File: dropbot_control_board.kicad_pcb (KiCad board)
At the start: 4 copper layers, 84 x 92 mm, 130 parts, among them IC1 MCP6024, J1 TFM-105-02-X-DH, P1 CONN_01X01, P2 CONN_01X01, P3 CONN_01X04, P4 CONN_01X04, P5 CONN_01X01, P7 CONN_01X04, P8 CONN_01X03, Q1 STP33N65M2, Q5 IRF740BPBF, Q6 IRF740BPBF, U1 Teensy_3.2, U10 W25Q64FV, U2 MAX1771, U3 CAT5171, U4 HV7802, U5 DPST (2 Form A), 350V, U6 NCP5304, U7 DPST (2 Form A), 350V, U8 DPST (2 Form A), 350V, U9 74AHC1G32

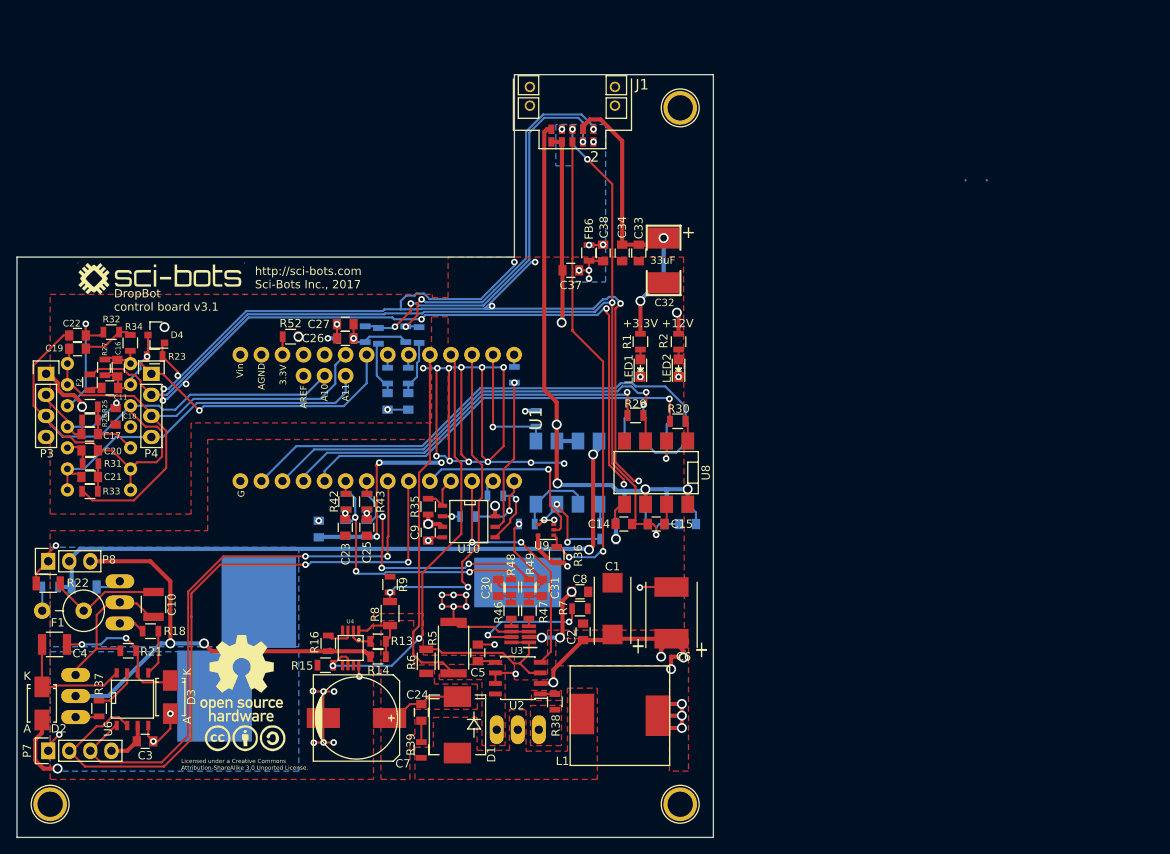
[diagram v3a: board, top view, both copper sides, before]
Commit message: Add usb passthrough, reset button, ...
* add usb passthrough
* add reset button
* fix bad trace on U5
* fix part number for C7 (3.3uF instead of 10uF)
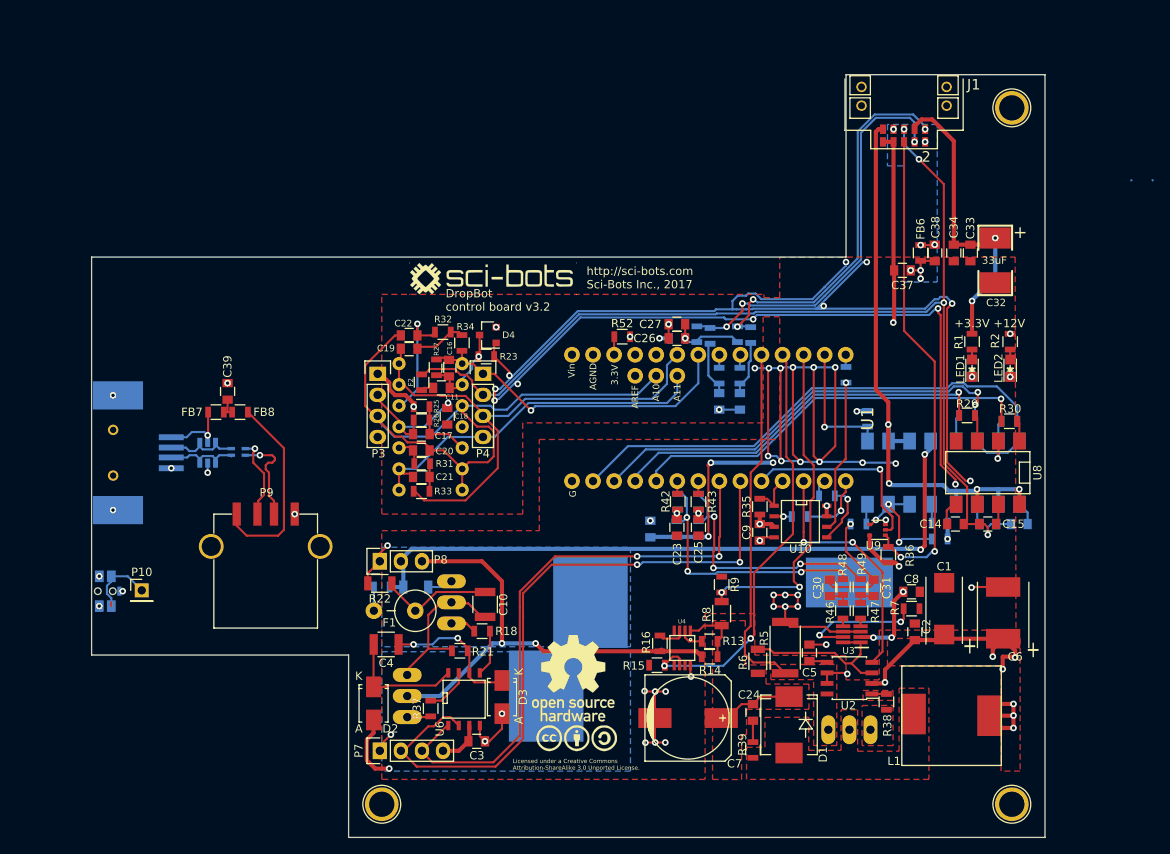
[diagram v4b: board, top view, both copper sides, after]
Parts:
- added C39: 0.1uF, Capacitors_SMD:C_0805, F.Cu at (49.4, 59.2)
- added D5: WE-TVS_824015, WheelerLab:wurth-WE-TVS_SOT23-6L, B.Cu at (47.0, 66.6)
- added FB7: 600 Ohm@100MHz, Resistors_SMD:R_0805, F.Cu at (48.0, 61.7)
- added FB8: 600 Ohm@100MHz, Resistors_SMD:R_0805, F.Cu at (50.9, 61.7)
- added L2: 90 Ohm@100MHz, WheelerLab:wurth-WE-CNSW_0805, B.Cu at (50.7, 66.5)
- added P10: CONN_01X01, Pin_Headers:Pin_Header_Straight_1x01_Pitch2.54mm, F.Cu at (39.0, 83.2)
- added P6: USB_B, WheelerLab:1734346-1, B.Cu at (35.6, 66.6)
- added P9: USB_A, WheelerLab:AU-Y1006, F.Cu at (54.0, 74.0)
- added SW1: PROG, WheelerLab:PTS840_GK_SMTR_LFS, B.Cu at (34.6, 83.3)
- C23, C25, C30, C31: value C_Small -> C
- R19, R20, R3, R4: value 4.75k -> 2k
- R40, R41, R42, R43, R44, R45, R46, R47, R48, R49, R50, R51: value R -> 0R
- moved C2 40.0 mm to (132.3, 88.2), turned to 270 degrees
- moved C37 40.0 mm to (130.8, 44.6)
- moved LED2 40.0 mm to (143.8, 56.4)
- moved R10 40.0 mm to (135.3, 77.0)
- moved R12 40.0 mm to (135.3, 75.1)
- moved R2 40.0 mm to (143.8, 53.2)
- moved C18 40.0 mm to (75.9, 62.2)
- moved C36 40.0 mm to (100.4, 75.8)
- moved G*** 40.0 mm to (81.4, 45.6)
- moved Q6 40.0 mm to (76.4, 84.6)
- moved R16 40.0 mm to (101.5, 89.6)
- moved R31 40.0 mm to (72.9, 67.9)
- moved R32 40.0 mm to (75.4, 52.0)
- moved R37 40.0 mm to (73.9, 97.5)
- moved U6 40.0 mm to (77.9, 96.3)
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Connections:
- C2 pad 1: +12V -> GND
- C2 pad 2: GND -> +12V
- U5 pad 2: Net-(R11-Pad2) -> Net-(R10-Pad2)
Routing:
- net Net-(FB8-Pad2): track 0.00 -> 23.9 mm
- net D+: track 0.00 -> 11.9 mm, vias 0 -> 1
- net Net-(D5-Pad4): track 0.00 -> 10.5 mm
- net CHASIS_GND: track 1.77 -> 12.1 mm, vias 2 -> 10
- net D-: track 0.00 -> 10.0 mm, vias 0 -> 1
- net Net-(D5-Pad1): track 0.00 -> 9.96 mm
- net Net-(D5-Pad5): track 0.00 -> 8.49 mm, vias 0 -> 1
- net Net-(P10-Pad1): track 0.00 -> 8.41 mm
- net Net-(R11-Pad2): track 9.47 -> 2.45 mm
- net +12V: track 82.3 -> 79.7 mm
- net Net-(R10-Pad2): track 12.9 -> 15.4 mm
- net Net-(C39-Pad2): track 0.00 -> 2.50 mm
- net GND: vias 47 -> 48
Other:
- board size 84 x 92 mm -> 115 x 92 mm
- net class PWR: via_dia 1.2 -> 0.8; via_drill 0.8 -> 0.4
- board text added: "DropBot control board v3.2"
- board text removed: "DropBot control board v3.1"

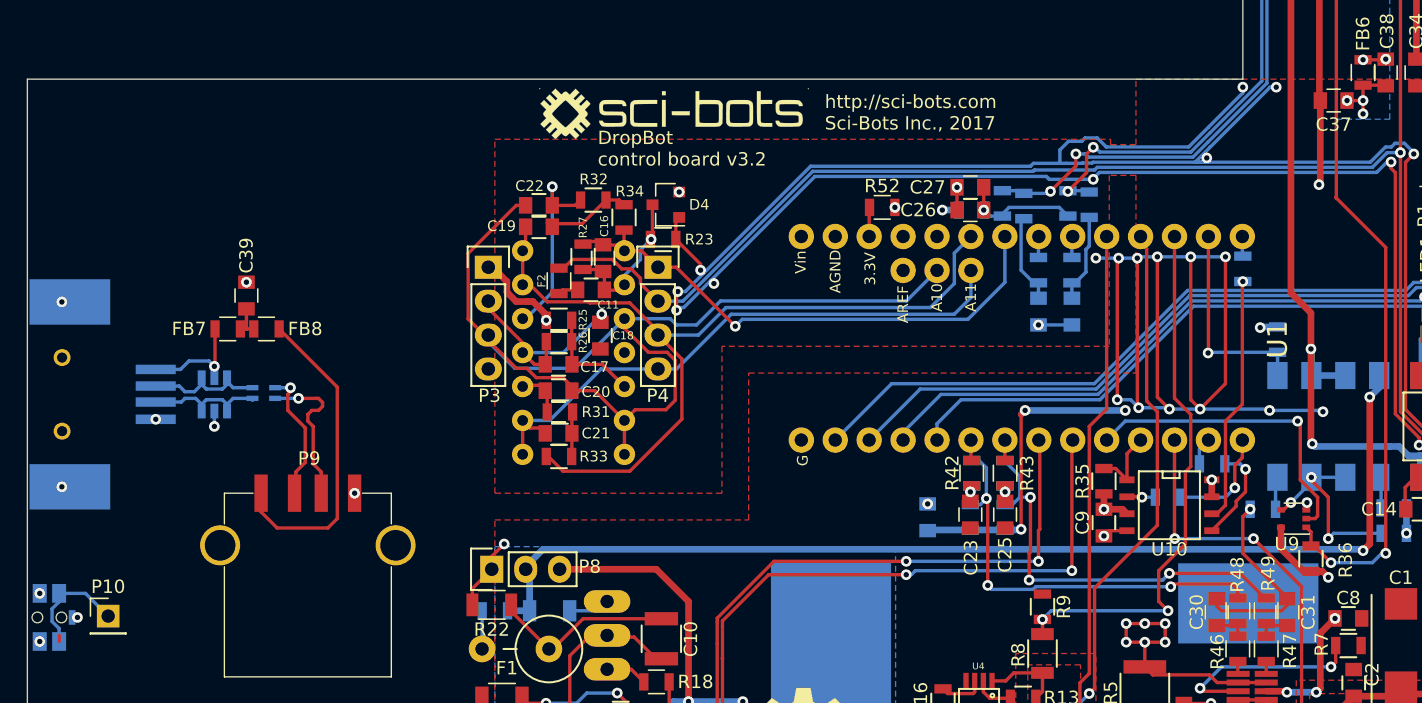
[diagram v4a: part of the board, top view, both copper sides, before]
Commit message: Swap F2 for higher voltage rating, monitor HV_OE
* swap F2 for 1210 footprint: B59807A90A62 (higher voltage rating)
* monitor HV_OE with A8
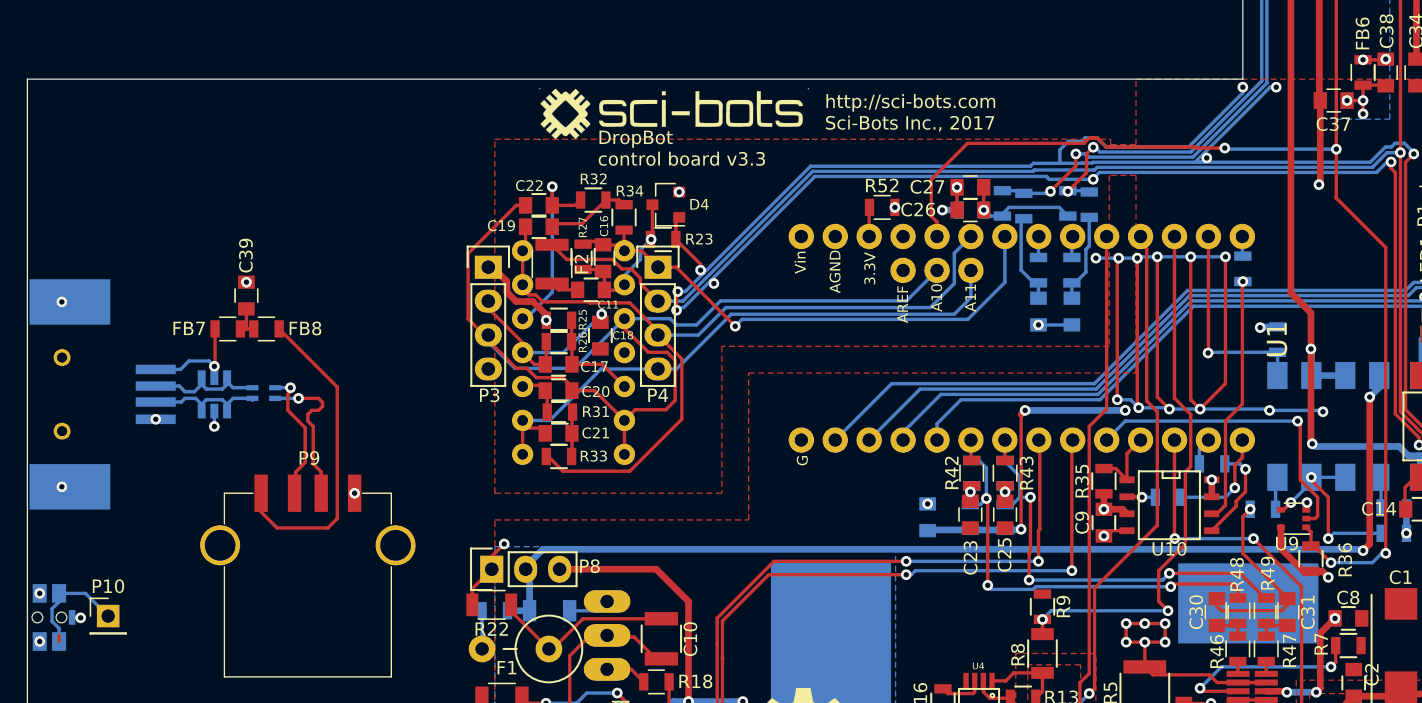
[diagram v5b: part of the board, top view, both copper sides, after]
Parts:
- F2: footprint Resistors_SMD:R_0805 -> Resistors_SMD:R_1210
- moved F2 1.35 mm to (72.3, 56.9)
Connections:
- U1 pad 22: Net-(U1-Pad22) -> HV_OE
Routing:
- net HV_OE: track 59.2 -> 95.6 mm, vias 2 -> 4
- net Net-(C11-Pad2): track 1.51 -> 2.12 mm
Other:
- board text added: "DropBot control board v3.3"
- board text removed: "DropBot control board v3.2"

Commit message: Change part numbers for i2c filters
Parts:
- C23, C25, C28, C29, C30, C31: value C -> 150pF
- R40, R41, R48, R49, R50, R51: value 0R -> 150
- R42, R43, R44, R45, R46, R47: value 0R -> 51
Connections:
- SW1 pad 3: CHASIS_GND -> (no net)
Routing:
- net (no net): track 83.8 -> 84.5 mm, vias 12 -> 13
- net CHASIS_GND: track 12.4 -> 11.7 mm, vias 10 -> 9
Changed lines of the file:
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@@
 (kicad_pcb (version 4) (host pcbnew 4.0.1-stable)
   (general
-    (links 298)
+    (links 297)
     (no_connects 0)
     (area 26.278199 20.326899 161.254002 113.050001)
@@
       (effects (font (size 1 1) (thickness 0.15)))
     )
-    (fp_text value C (at 0 1.75 270) (layer F.Fab)
+    (fp_text value 150pF (at 0 1.75 270) (layer F.Fab)
       (effects (font (size 1 1) (thickness 0.15)))
     )
@@
       (effects (font (size 1 1) (thickness 0.15)))
     )
-    (fp_text value C (at 0 1.75 90) (layer F.Fab)
+    (fp_text value 150pF (at 0 1.75 90) (layer F.Fab)
       (effects (font (size 1 1) (thickness 0.15)))
     )
@@
       (effects (font (size 1 1) (thickness 0.15)) (justify mirror))
     )
-    (fp_text value C (at 0 -1.75 270) (layer B.Fab)
+    (fp_text value 150pF (at 0 -1.75 270) (layer B.Fab)
       (effects (font (size 1 1) (thickness 0.15)) (justify mirror))
     )
@@
       (effects (font (size 1 1) (thickness 0.15)) (justify mirror))
     )
-    (fp_text value C (at 0 -1.75 90) (layer B.Fab)
+    (fp_text value 150pF (at 0 -1.75 90) (layer B.Fab)
       (effects (font (size 1 1) (thickness 0.15)) (justify mirror))
     )
@@
       (effects (font (size 1 1) (thickness 0.15)))
     )
-    (fp_text value C (at 0 1.75 90) (layer F.Fab)
+    (fp_text value 150pF (at 0 1.75 90) (layer F.Fab)
       (effects (font (size 1 1) (thickness 0.15)))
     )
@@
       (effects (font (size 1 1) (thickness 0.15)))
     )
-    (fp_text value C (at 0 1.75 270) (layer F.Fab)
+    (fp_text value 150pF (at 0 1.75 270) (layer F.Fab)
       (effects (font (size 1 1) (thickness 0.15)))
     )
@@
       (effects (font (size 1 1) (thickness 0.15)) (justify mirror))
     )
-    (fp_text value 0R (at 0 0 90) (layer B.Fab)
+    (fp_text value 150 (at 0 0 90) (layer B.Fab)
       (effects (font (size 1 1) (thickness 0.15)) (justify mirror))
     )
@@
       (effects (font (size 1 1) (thickness 0.15)) (justify mirror))
     )
-    (fp_text value 0R (at 0 0 90) (layer B.Fab)
+    (fp_text value 150 (at 0 0 90) (layer B.Fab)
       (effects (font (size 1 1) (thickness 0.15)) (justify mirror))
     )
@@
       (effects (font (size 1 1) (thickness 0.15)))
     )
-    (fp_text value 0R (at 0 1.75 270) (layer F.Fab)
+    (fp_text value 51 (at 0 1.75 270) (layer F.Fab)
       (effects (font (size 1 1) (thickness 0.15)))
     )
@@
       (effects (font (size 1 1) (thickness 0.15)))
     )
-    (fp_text value 0R (at 0 1.75 270) (layer F.Fab)
+    (fp_text value 51 (at 0 1.75 270) (layer F.Fab)
       (effects (font (size 1 1) (thickness 0.15)))
     )
@@
       (effects (font (size 1 1) (thickness 0.15)) (justify mirror))
     )
-    (fp_text value 0R (at 0 -1.75 90) (layer B.Fab)
+    (fp_text value 51 (at 0 -1.75 90) (layer B.Fab)
       (effects (font (size 1 1) (thickness 0.15)) (justify mirror))
     )
@@
       (effects (font (size 1 1) (thickness 0.15)) (justify mirror))
     )
-    (fp_text value 0R (at 0 -1.75 90) (layer B.Fab)
+    (fp_text value 51 (at 0 -1.75 90) (layer B.Fab)
       (effects (font (size 1 1) (thickness 0.15)) (justify mirror))
     )
@@
       (effects (font (size 1 1) (thickness 0.15)))
     )
-    (fp_text value 0R (at 0 1.75 270) (layer F.Fab)
+    (fp_text value 51 (at 0 1.75 270) (layer F.Fab)
       (effects (font (size 1 1) (thickness 0.15)))
     )
@@
       (effects (font (size 1 1) (thickness 0.15)))
     )
-    (fp_text value 0R (at 0 1.75 270) (layer F.Fab)
+    (fp_text value 51 (at 0 1.75 270) (layer F.Fab)
       (effects (font (size 1 1) (thickness 0.15)))
     )
@@
       (effects (font (size 1 1) (thickness 0.15)))
     )
-    (fp_text value 0R (at 0 1.75 270) (layer F.Fab)
+    (fp_text value 150 (at 0 1.75 270) (layer F.Fab)
       (effects (font (size 1 1) (thickness 0.15)))
     )
@@
       (effects (font (size 1 1) (thickness 0.15)))
     )
-    (fp_text value 0R (at 0 1.75 270) (layer F.Fab)
+    (fp_text value 150 (at 0 1.75 270) (layer F.Fab)
       (effects (font (size 1 1) (thickness 0.15)))
     )
@@
       (effects (font (size 1 1) (thickness 0.15)) (justify mirror))
     )
-    (fp_text value 0R (at 0 -1.75 270) (layer B.Fab)
+    (fp_text value 150 (at 0 -1.75 270) (layer B.Fab)
       (effects (font (size 1 1) (thickness 0.15)) (justify mirror))
     )
@@
       (effects (font (size 1 1) (thickness 0.15)) (justify mirror))
     )
-    (fp_text value 0R (at 0 -1.75 270) (layer B.Fab)
+    (fp_text value 150 (at 0 -1.75 270) (layer B.Fab)
       (effects (font (size 1 1) (thickness 0.15)) (justify mirror))
     )
@@
     (fp_line (start -1.75 -1.45) (end 1.75 -1.45) (layer B.SilkS) (width 0.12))
     (fp_line (start -1.75 1.45) (end 1.75 1.45) (layer B.SilkS) (width 0.12))
-    (pad 3 smd rect (at 0 1.7 90) (size 1.1 0.5) (layers Back F.Adhes B.Paste B.Mask)
-      (net 94 CHASIS_GND))
+    (pad 3 smd rect (at 0 1.7 90) (size 1.1 0.5) (layers Back F.Adhes B.Paste B.Mask))
     (pad "" np_thru_hole circle (at 0 -0.9 90) (size 0.8 0.8) (drill 0.8) (layers *.Cu *.Mask B.SilkS))
     (pad 2 smd rect (at 1.8 -0.725 90) (size 1.4 1.05) (layers Back B.Paste B.Mask)
@@
   (via (at 114.7 56.4) (size 0.8) (drill 0.4) (layers Front Back) (net 0))
   (segment (start 35.375 85.1) (end 35.375 84.625) (width 0.254) (layer Front) (net 0))
+  (segment (start 36.35 83.3) (end 36.96 83.3) (width 0.254) (layer Back) (net 0))
+  (via (at 36.99 83.33) (size 0.8) (drill 0.4) (layers Front Back) (net 0))
+  (segment (start 36.96 83.3) (end 36.99 83.33) (width 0.254) (layer Back) (net 0))
   (via (at 57.5 74) (size 0.8) (drill 0.4) (layers Front Back) (net 1))
   (segment (start 133 43.45) (end 133 44.6) (width 0.254) (layer Front) (net 1))
@@
   (segment (start 123.964 54.78) (end 123.964 56.214) (width 0.254) (layer Back) (net 93))
   (segment (start 123.964 56.214) (end 124 56.25) (width 0.254) (layer Back) (net 93))
-  (segment (start 36.35 83.3) (end 36.96 83.3) (width 0.254) (layer Back) (net 94))
-  (via (at 36.99 83.33) (size 0.8) (drill 0.4) (layers Front Back) (net 94))
-  (segment (start 36.96 83.3) (end 36.99 83.33) (width 0.254) (layer Back) (net 94))
   (segment (start 33.925 81.5) (end 33.925 75.17689) (width 0.254) (layer GND) (net 94))
   (segment (start 35.6 73.50189) (end 35.58166 73.52023) (width 0.254) (layer Front) (net 94))

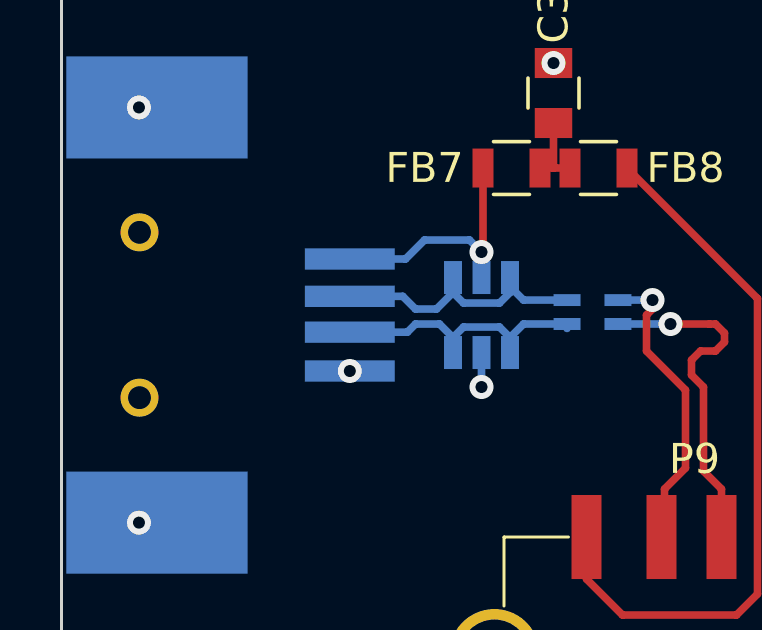
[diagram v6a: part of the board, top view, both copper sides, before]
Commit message: [WIP] Fix USB-B footprint (P6)
Fixes #3
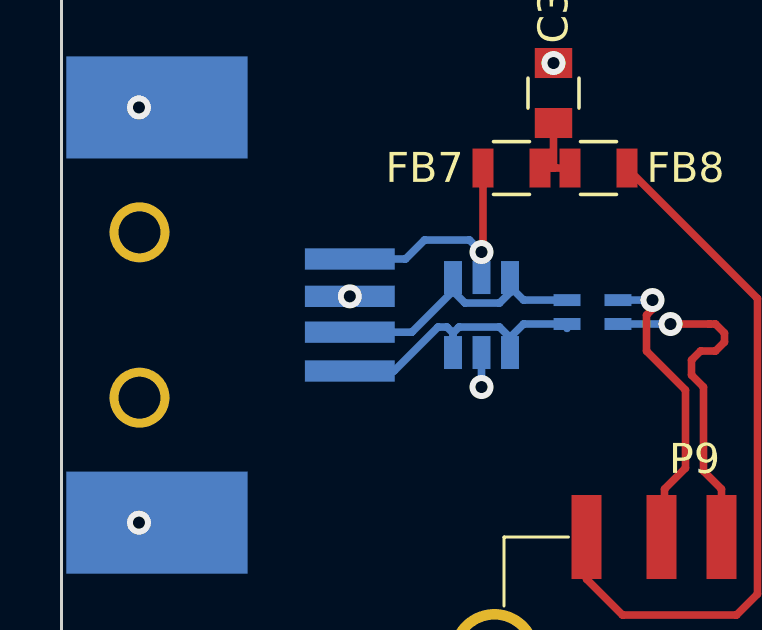
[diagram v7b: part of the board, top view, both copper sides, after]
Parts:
- C6: value 100uF,35V -> 100uF
- D1: value ES3J -> 400V, 4A, <50ns
- F2: value PTC 30mA -> PTC 15mA
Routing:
- net Net-(D5-Pad1): track 9.96 -> 11.4 mm
